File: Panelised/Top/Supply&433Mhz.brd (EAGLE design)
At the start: 65 x 56.5 mm, 17 parts, among them K1 61004021821, P1 DF11-06-2DSA, Q1 BS170

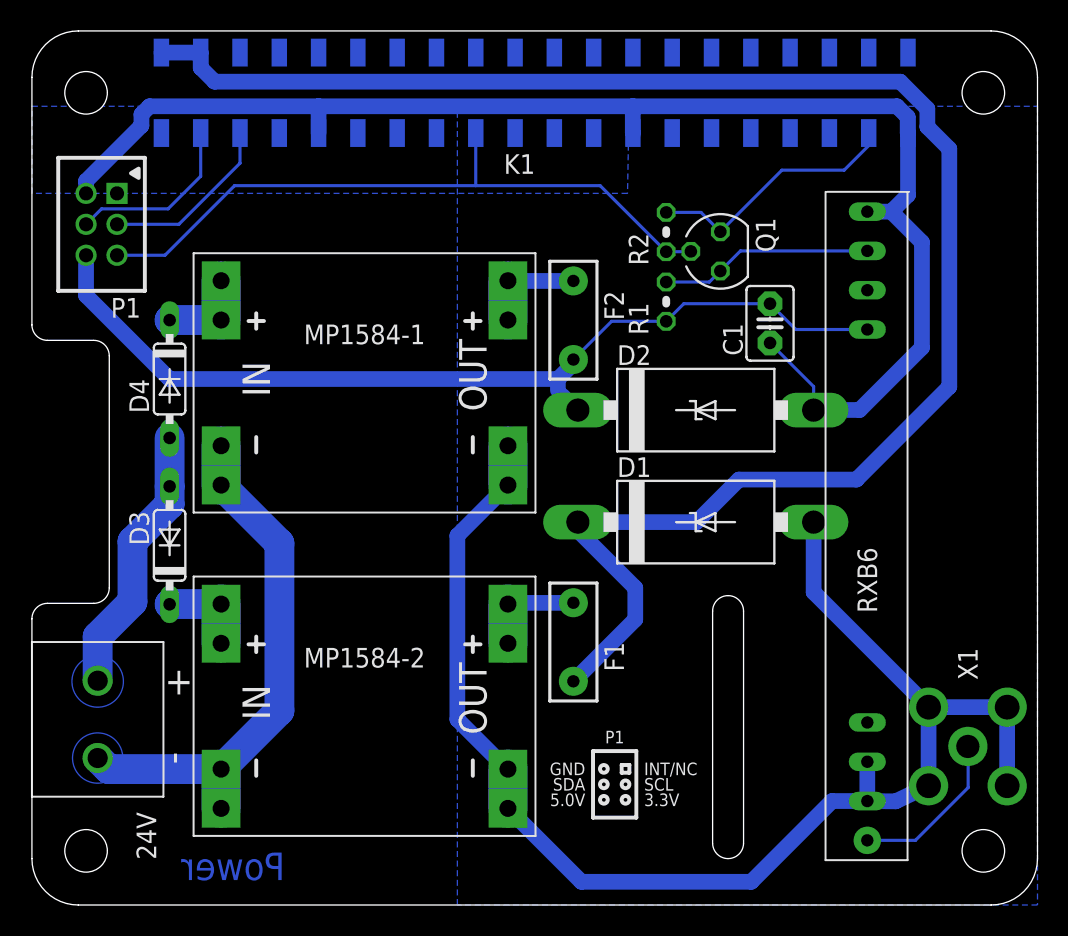
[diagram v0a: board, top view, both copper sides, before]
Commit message: Remove AGND supply, since DC/DC converter use same GND signal.
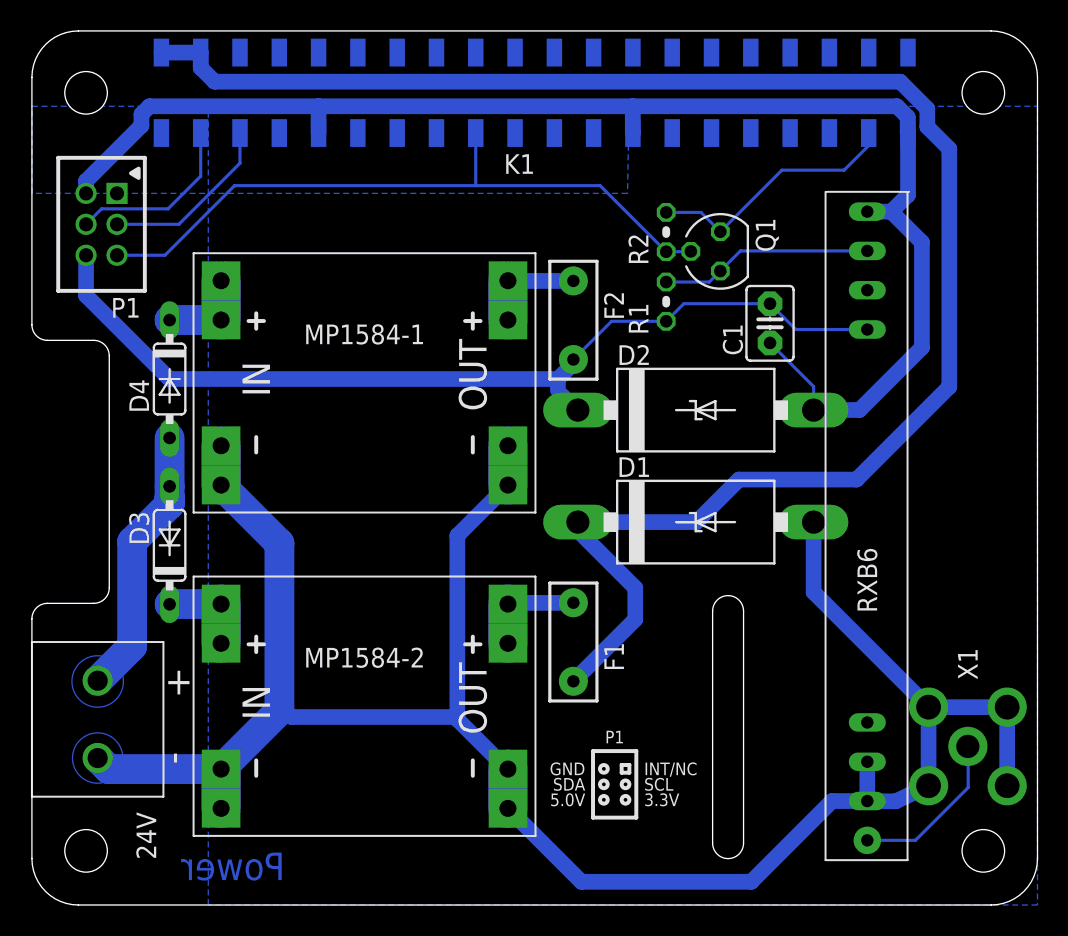
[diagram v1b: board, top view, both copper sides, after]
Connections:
- removed net AGND: 24V.1, MP1584-1.IN-0, MP1584-1.IN-1, MP1584-2.IN-0, MP1584-2.IN-1
- net GND: now also 24V.1, MP1584-1.IN-0, MP1584-1.IN-1, MP1584-2.IN-0, MP1584-2.IN-1
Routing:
- net GND: track 182.5 -> 229.3 mm
- net AGND: track 35.1 -> 0.00 mm
- net +24V: track 17.6 -> 18.1 mm
- removed copper zone on layer 16, net AGND
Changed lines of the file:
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@@
 <contactref element="MP1584-1" pad="OUT-0"/>
 <polygon width="1.016" layer="16" isolate="0.4064" thermals="no">
-<vertex x="27.5" y="0"/>
-<vertex x="27.5" y="51.63"/>
+<vertex x="11.4" y="0"/>
+<vertex x="11.4" y="51.63"/>
 <vertex x="65" y="51.63"/>
 <vertex x="65" y="0"/>
@@
 <vertex x="0" y="51.63"/>
 </polygon>
-</signal>
-<signal name="+24V">
-<contactref element="D3" pad="A"/>
-<contactref element="D4" pad="A"/>
-<contactref element="24V" pad="2"/>
-<polygon width="0.35" layer="16" isolate="0.254" thermals="no">
-<vertex x="3.15" y="13.2" curve="180"/>
-<vertex x="5.35" y="15.7" curve="180"/>
-</polygon>
-<wire x1="4.25" y1="17.35" x2="6.5" y2="19.6" width="1.9304" layer="16"/>
-<wire x1="6.5" y1="19.6" x2="6.5" y2="23.5" width="1.9304" layer="16"/>
-<wire x1="6.5" y1="23.5" x2="8.9" y2="25.9" width="1.9304" layer="16"/>
-<wire x1="8.9" y1="25.9" x2="8.9" y2="27.06" width="1.9304" layer="16"/>
-<wire x1="4.25" y1="14.5" x2="4.25" y2="17.35" width="1.9304" layer="16"/>
-<wire x1="8.9" y1="30.19" x2="8.9" y2="27.06" width="1.9304" layer="16"/>
-</signal>
-<signal name="AGND">
 <contactref element="MP1584-2" pad="IN-0"/>
 <contactref element="MP1584-1" pad="IN-0"/>
 <contactref element="24V" pad="1"/>
-<polygon width="0.35" layer="16" thermals="no">
-<vertex x="3.15" y="8.3" curve="180"/>
-<vertex x="5.35" y="10.7" curve="180"/>
-</polygon>
 <contactref element="MP1584-2" pad="IN-1"/>
 <contactref element="MP1584-1" pad="IN-1"/>
@@
 <wire x1="12.229" y1="27.146" x2="16" y2="23.375" width="1.9304" layer="16"/>
 <wire x1="16" y1="23.375" x2="16" y2="12.557" width="1.9304" layer="16"/>
+<wire x1="27.1624" y1="12.1516" x2="16.7978" y2="12.1516" width="1.016" layer="16"/>
+<wire x1="16.7978" y1="12.1516" x2="16" y2="12.557" width="1.016" layer="16"/>
+<wire x1="27.1624" y1="12.1516" x2="27.5" y2="12" width="0.1524" layer="16"/>
+<polygon width="0.35" layer="16" thermals="no">
+<vertex x="3.15" y="8.3" curve="180"/>
+<vertex x="5.35" y="10.7" curve="180"/>
+</polygon>
+</signal>
+<signal name="+24V">
+<contactref element="D3" pad="A"/>
+<contactref element="D4" pad="A"/>
+<contactref element="24V" pad="2"/>
+<polygon width="0.35" layer="16" isolate="0.254" thermals="no">
+<vertex x="3.15" y="13.2" curve="180"/>
+<vertex x="5.35" y="15.7" curve="180"/>
+</polygon>
+<wire x1="8.9" y1="25.9" x2="8.9" y2="26.4" width="1.9304" layer="16"/>
+<wire x1="8.9" y1="26.4" x2="8.9" y2="27.06" width="1.9304" layer="16"/>
+<wire x1="8.9" y1="30.19" x2="8.9" y2="27.06" width="1.9304" layer="16"/>
+<wire x1="4.25" y1="14.5" x2="6.48" y2="16.73" width="1.9304" layer="16"/>
+<wire x1="6.48" y1="16.73" x2="6.48" y2="23.48" width="1.9304" layer="16"/>
+<wire x1="6.48" y1="23.48" x2="8.9" y2="25.9" width="1.9304" layer="16"/>
+<wire x1="8.9" y1="25.9" x2="8.9" y2="26.4" width="1.9304" layer="16"/>
 </signal>
 <signal name="N$2">

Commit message: Increase ground plane.
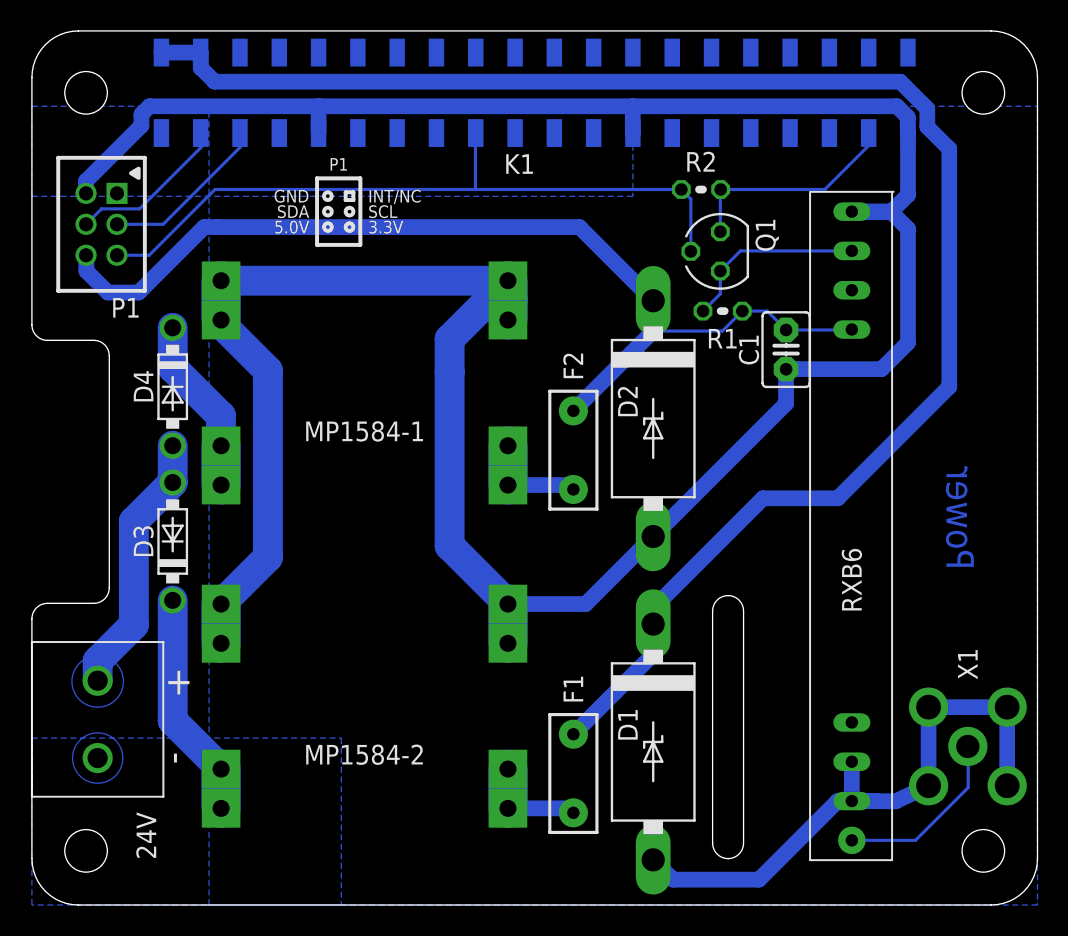
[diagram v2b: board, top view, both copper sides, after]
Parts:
- D3, D4: value 1N4148DO35-7 -> SB160; device diode:DO35-7 -> diode:DO41-7.6
- moved D1 14.5 mm to (40.2, 10.5), turned to 270 degrees
- moved F1 8.50 mm to (35.0, 8.50), turned to 270 degrees
- moved F2 8.40 mm to (35.0, 29.4), turned to 90 degrees
- moved R1 3.70 mm to (44.6, 38.4), turned to 180 degrees
- moved R2 3.55 mm to (43.2, 46.2), turned to 180 degrees
- moved D2 2.80 mm to (40.2, 31.4), turned to 270 degrees
- moved C1 1.99 mm to (48.8, 35.9)
- moved RXB6 1.00 mm to (53.0, 24.5)
- moved D4 0.54 mm to (9.10, 33.5)
- moved D3 0.32 mm to (9.10, 23.5)
- flipped MP1584-1 to the bottom, turned to 180 degrees
- flipped MP1584-2 to the bottom, turned to 180 degrees
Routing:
- net N$7: track 5.89 -> 14.8 mm
- net N$5: track 111.3 -> 105.5 mm
- net N$9: track 5.87 -> 11.5 mm
- net N$2: track 60.8 -> 65.1 mm
- net N$69: track 16.7 -> 14.3 mm
- net N$11: track 44.3 -> 46.3 mm
- net N$3: track 13.8 -> 12.1 mm
- net N$12: track 11.5 -> 10.4 mm
- net N$8: track 10.6 -> 11.6 mm
- net +24V: track 18.1 -> 17.2 mm
- net GND: track 229.3 -> 228.5 mm
- net N$1: track 11.5 -> 11.0 mm

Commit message: Use SB1H100 as protection diode instead of SB160.
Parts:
- D3, D4: value SB160 -> SB1H100
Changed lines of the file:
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@@
 <attribute name="VALUE" x="21.5" y="35.95" size="1.27" layer="27" rot="R180" align="top-center"/>
 </element>
-<element name="D3" library="diode" package="DO41-7.6" value="SB160" x="9.1" y="23.5" smashed="yes" rot="R90">
+<element name="D3" library="diode" package="DO41-7.6" value="SB1H100" x="9.1" y="23.5" smashed="yes" rot="R90">
 <attribute name="NAME" x="7.85" y="23.5" size="1.27" layer="25" font="vector" ratio="10" rot="R90" align="bottom-center"/>
 <attribute name="VALUE" x="11.767" y="21.214" size="1.27" layer="27" ratio="10" rot="R90"/>
 </element>
-<element name="D4" library="diode" package="DO41-7.6" value="SB160" x="9.1" y="33.5" smashed="yes" rot="R270">
+<element name="D4" library="diode" package="DO41-7.6" value="SB1H100" x="9.1" y="33.5" smashed="yes" rot="R270">
 <attribute name="NAME" x="7.85" y="33.5" size="1.27" layer="25" font="vector" ratio="10" rot="R270" align="top-center"/>
 <attribute name="VALUE" x="6.433" y="35.786" size="1.27" layer="27" ratio="10" rot="R270"/>
